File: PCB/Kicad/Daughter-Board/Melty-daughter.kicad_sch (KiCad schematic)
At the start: 7 parts, among them J1 Conn_01x07_Female, Q1 SFH 325

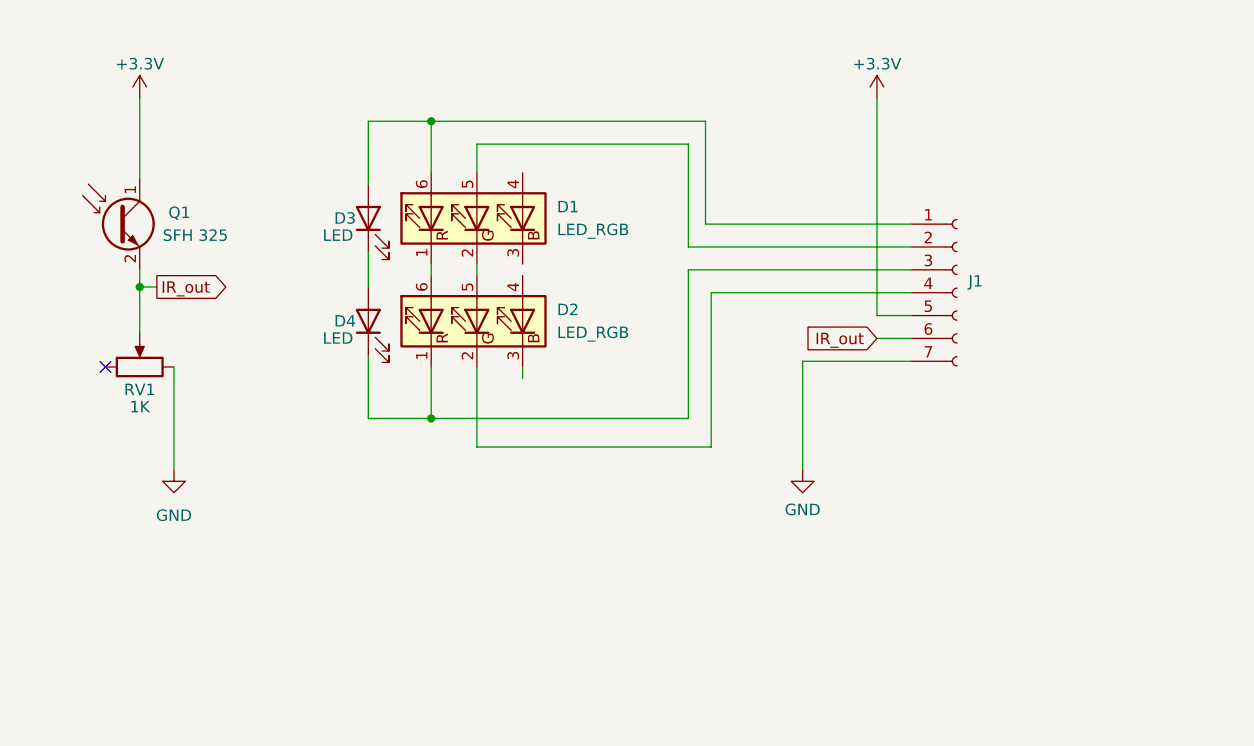
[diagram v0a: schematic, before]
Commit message: Add IR Board schematic and PCB design
Add kicad files for the schematic and PCB of the IR Board.
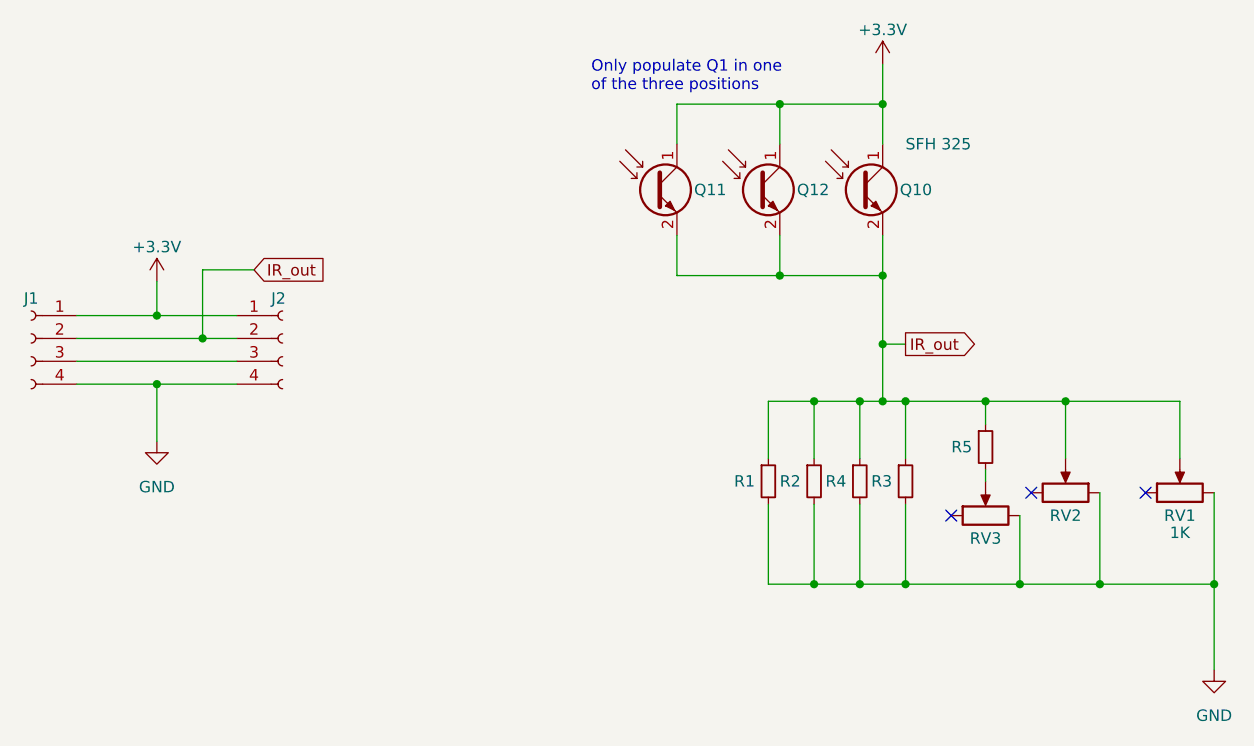
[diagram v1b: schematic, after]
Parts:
- removed D1, D2: LED_RGB, KiCad:LED_RGB_Harvatek_B3803FCH, symbol Device:LED_RGB
- removed D3, D4: LED, LED_THT:LED_D3.0mm, symbol Device:LED
- removed J1: Conn_01x07_Female, Connector_PinSocket_2.00mm:PinSocket_1x07_P2.00mm_Vertical, symbol Connector:Conn_01x07_Female
- added J1, J2: Conn_01x04_Female, Connector_PinHeader_2.54mm:PinHeader_1x04_P2.54mm_Vertical, symbol Connector:Conn_01x04_Female
- added Q11, Q12: SFH 325, KiCad:SFH325FA34Z, symbol Device:Q_Photo_NPN
- added R1: R, Resistor_SMD:R_0603_1608Metric_Pad0.98x0.95mm_HandSolder, symbol Device:R_Small
- added R2, R4: R_Small, Resistor_SMD:R_0805_2012Metric_Pad1.20x1.40mm_HandSolder, symbol Device:R_Small
- added R3, R5: R_Small, Resistor_THT:R_Axial_DIN0204_L3.6mm_D1.6mm_P7.62mm_Horizontal, symbol Device:R_Small
- added RV2: 1K, Connector_PinHeader_2.54mm:PinHeader_1x03_P2.54mm_Vertical, symbol Device:R_Potentiometer
- added RV3: 1K, KiCad:Potentiometer_Bourns_TC42_Horizontal, symbol Device:R_Potentiometer
- renumbered Q1 to Q10
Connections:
- net +3V3: now also J1.1 (Pin_1), J2.1 (Pin_1), Q11.1 (C), Q12.1 (C)
- net GND: now also J1.4 (Pin_4), J2.4 (Pin_4), R1.2, R2.2, R3.2, R4.2, RV2.1, RV3.3
- net IR_out: now also J1.2 (Pin_2), J2.2 (Pin_2), Q11.2 (E), Q12.2 (E), R1.1, R2.1, R3.1, R4.1, R5.1, RV2.2
- new net: J1.3 (Pin_3), J2.3 (Pin_3)
- new net: R5.2, RV3.2
- no-connect marks 1 -> 3
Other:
- note added: "Only populate Q1 in one of the three positions"
- title: (none) -> Oreo IR Board
- moved on the sheet: Q10, RV1
